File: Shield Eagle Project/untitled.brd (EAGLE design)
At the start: 160 x 100 mm, 5 parts, among them IC1 MCP4922-E_P, J1 61PC6F, Q1 TLP222A-2_F_, U1 ARDUINOR3-BPLACE

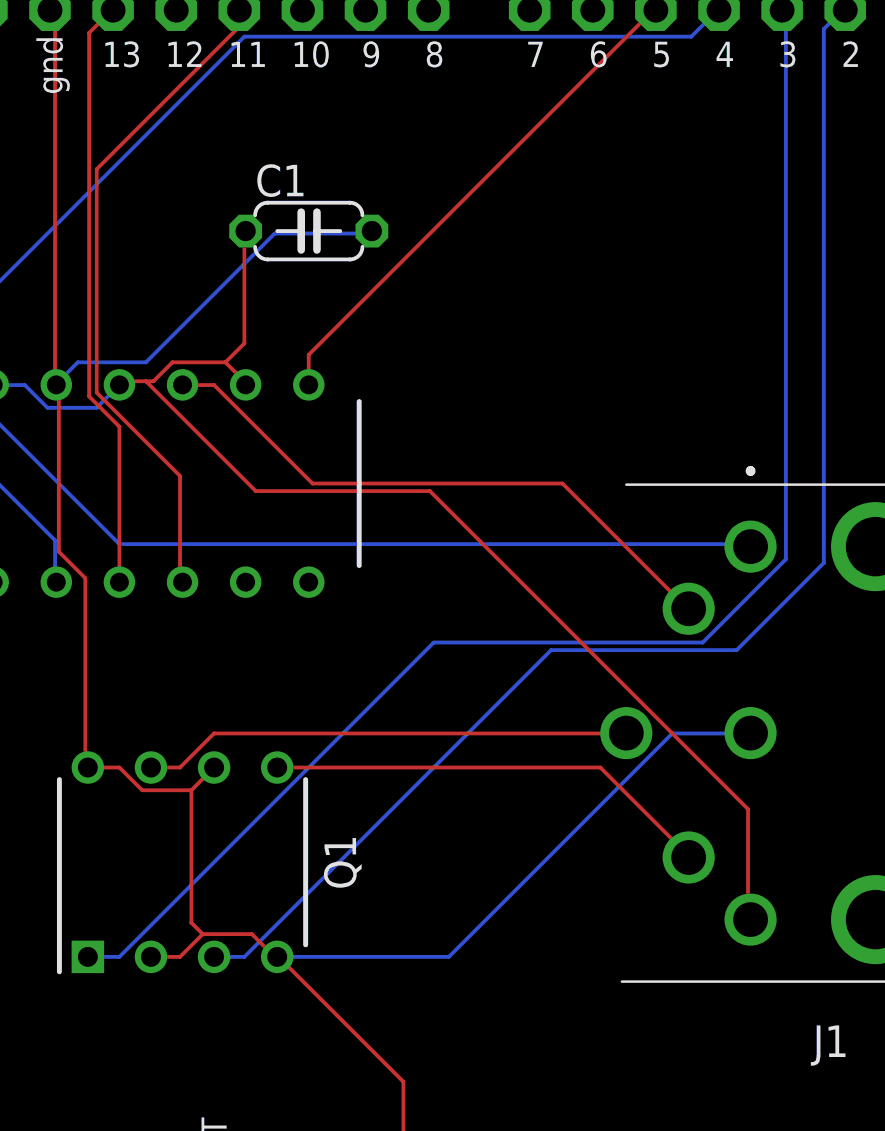
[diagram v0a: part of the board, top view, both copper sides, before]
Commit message: Add current limiting resistor for SSR to meet spec.
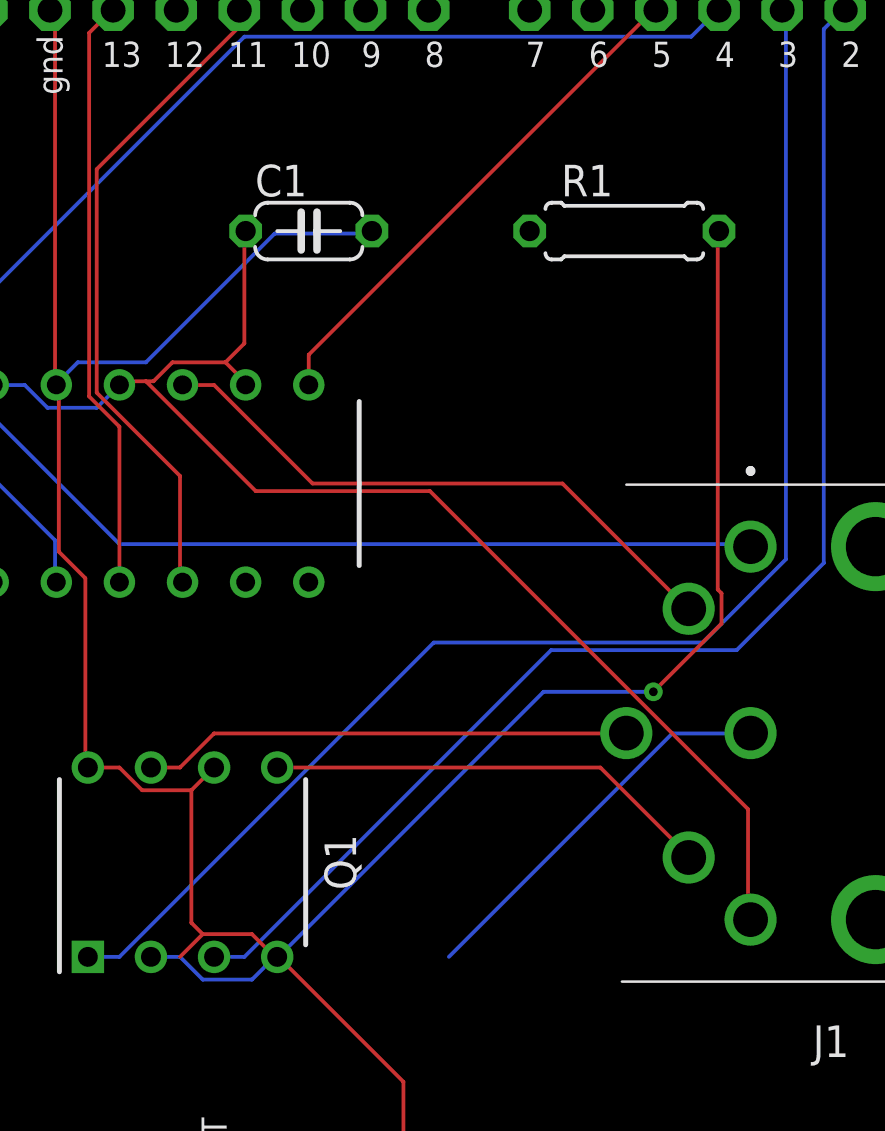
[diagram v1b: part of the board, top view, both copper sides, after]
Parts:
- added R1: 130 ohm, adafruit:0207/7
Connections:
- new net N$3: Q1.2, Q1.4, R1.2
- net GND: now also R1.1; no longer Q1.2, Q1.4
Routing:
- net N$3: track 0.00 -> 45.1 mm, vias 0 -> 1
- net GND: track 101.8 -> 93.6 mm
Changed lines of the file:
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@@
 <?xml version="1.0" encoding="utf-8"?>
 <!DOCTYPE eagle SYSTEM "eagle.dtd">
-<eagle version="9.6.1">
+<eagle version="9.6.2">
 <drawing>
 <settings>
@@
 <attribute name="VALUE" x="39.751" y="41.783" size="1.27" layer="27" ratio="10"/>
 </element>
+<element name="R1" library="adafruit" package="0207/7" value="130 ohm" x="54.61" y="44.45" smashed="yes">
+<attribute name="NAME" x="52.07" y="45.847" size="1.27" layer="25" ratio="10"/>
+<attribute name="VALUE" x="51.054" y="41.3512" size="1.27" layer="27" ratio="10"/>
+</element>
 </elements>
 <signals>
 <signal name="GND">
 <contactref element="U1" pad="GND1"/>
-<contactref element="Q1" pad="4"/>
-<contactref element="Q1" pad="2"/>
 <contactref element="IC1" pad="12"/>
 <contactref element="J1" pad="3"/>
@@
 <wire x1="48.1584" y1="5.1816" x2="45.72" y2="5.1816" width="0.1524" layer="1"/>
 <wire x1="48.1584" y1="5.1816" x2="48.26" y2="5.08" width="0.1524" layer="1"/>
-<wire x1="36.7284" y1="15.24" x2="35.56" y2="15.24" width="0.1524" layer="1"/>
 <wire x1="37.6428" y1="16.1544" x2="36.7284" y2="15.24" width="0.1524" layer="1"/>
 <wire x1="39.624" y1="16.1544" x2="37.6428" y2="16.1544" width="0.1524" layer="1"/>
 <wire x1="40.5384" y1="15.24" x2="39.624" y2="16.1544" width="0.1524" layer="1"/>
-<wire x1="40.5384" y1="15.24" x2="40.64" y2="15.24" width="0.1524" layer="1"/>
 <wire x1="45.72" y1="10.2108" x2="45.72" y2="5.1816" width="0.1524" layer="1"/>
 <wire x1="40.6908" y1="15.24" x2="45.72" y2="10.2108" width="0.1524" layer="1"/>
 <wire x1="45.72" y1="5.1816" x2="45.72" y2="5.08" width="0.1524" layer="1"/>
-<wire x1="40.6908" y1="15.24" x2="40.64" y2="15.24" width="0.1524" layer="1"/>
 <wire x1="56.5404" y1="24.2316" x2="59.5884" y2="24.2316" width="0.1524" layer="16"/>
 <wire x1="47.5488" y1="15.24" x2="56.5404" y2="24.2316" width="0.1524" layer="16"/>
-<wire x1="40.64" y1="15.24" x2="47.5488" y2="15.24" width="0.1524" layer="16"/>
 <wire x1="59.5884" y1="24.2316" x2="59.69" y2="24.245" width="0.1524" layer="16"/>
 <wire x1="37.1856" y1="16.6116" x2="37.1856" y2="21.9456" width="0.1524" layer="1"/>
@@
 <vertex x="5.08" y="2.54"/>
 </polygon>
+<contactref element="R1" pad="1"/>
 </signal>
 <signal name="VIN">
@@
 <wire x1="34.29" y1="38.2524" x2="34.29" y2="38.26" width="0.1524" layer="16"/>
 </signal>
+<signal name="N$3">
+<contactref element="Q1" pad="4"/>
+<contactref element="Q1" pad="2"/>
+<contactref element="R1" pad="2"/>
+<wire x1="36.7284" y1="15.24" x2="35.56" y2="15.24" width="0.1524" layer="16"/>
+<wire x1="37.6428" y1="14.3256" x2="36.7284" y2="15.24" width="0.1524" layer="16"/>
+<wire x1="39.624" y1="14.3256" x2="37.6428" y2="14.3256" width="0.1524" layer="16"/>
+<wire x1="40.5384" y1="15.24" x2="39.624" y2="14.3256" width="0.1524" layer="16"/>
+<wire x1="40.5384" y1="15.24" x2="40.64" y2="15.24" width="0.1524" layer="16"/>
+<wire x1="58.3692" y1="30.0228" x2="58.3692" y2="44.3484" width="0.1524" layer="1"/>
+<wire x1="58.5216" y1="29.8704" x2="58.3692" y2="30.0228" width="0.1524" layer="1"/>
+<wire x1="58.5216" y1="28.6512" x2="58.5216" y2="29.8704" width="0.1524" layer="1"/>
+<wire x1="55.7784" y1="25.908" x2="58.5216" y2="28.6512" width="0.1524" layer="1"/>
+<wire x1="51.3588" y1="25.908" x2="55.7784" y2="25.908" width="0.1524" layer="16"/>
+<wire x1="40.6908" y1="15.24" x2="51.3588" y2="25.908" width="0.1524" layer="16"/>
+<wire x1="58.3692" y1="44.3484" x2="58.42" y2="44.45" width="0.1524" layer="1"/>
+<wire x1="40.6908" y1="15.24" x2="40.64" y2="15.24" width="0.1524" layer="16"/>
+<via x="55.7784" y="25.908" extent="1-16" drill="0.35"/>
+</signal>
 </signals>

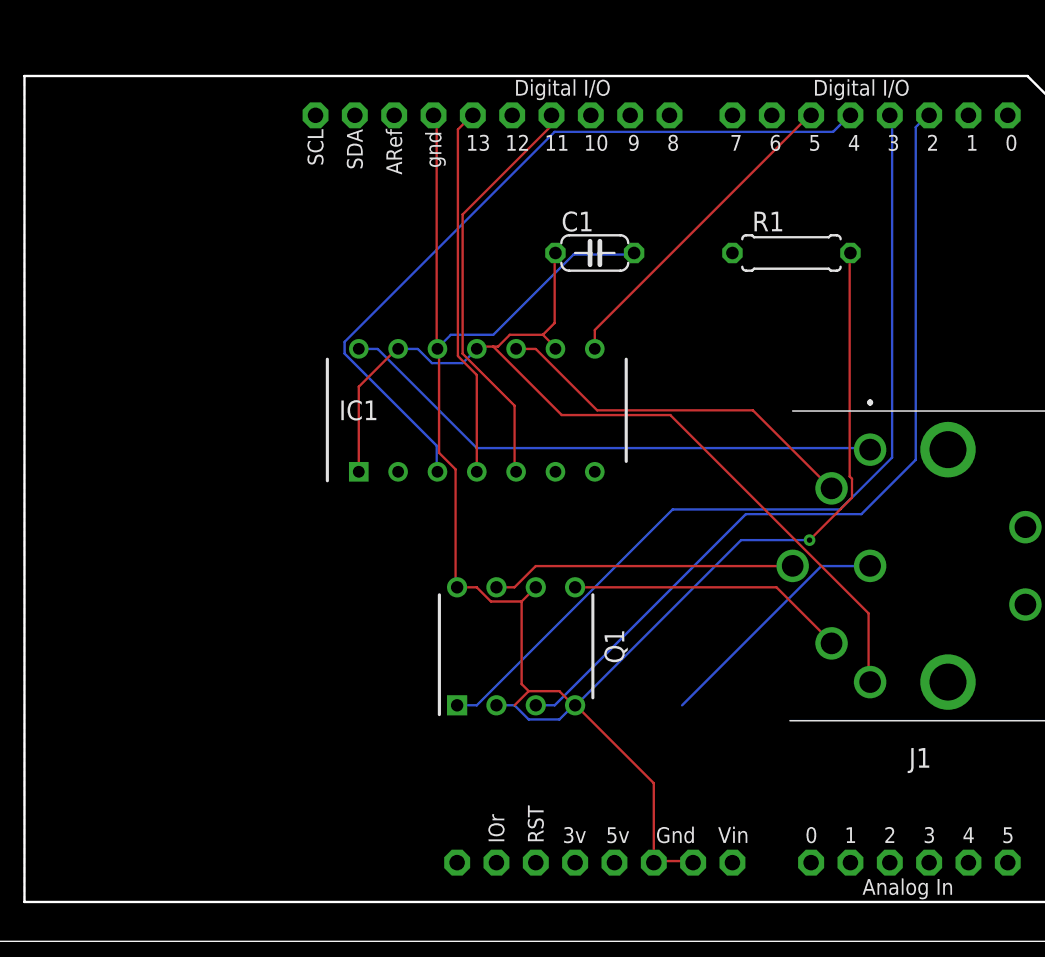
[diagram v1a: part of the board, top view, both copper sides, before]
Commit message: Using individual resistors between opto isolator and ground to avoid under current conditions that might have happened otherwise.
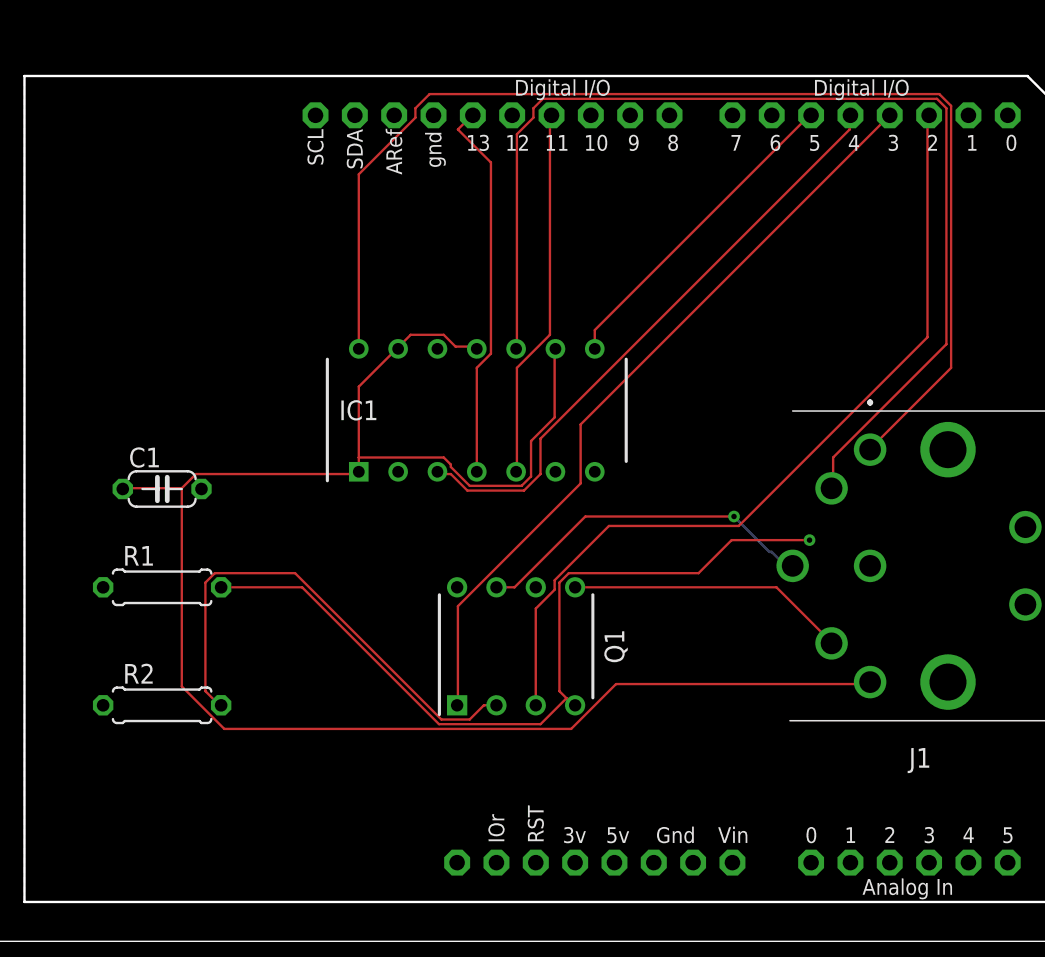
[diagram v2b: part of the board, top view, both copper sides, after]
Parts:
- added R2: 130 ohm, adafruit:0207/7
- moved R1 46.0 mm to (14.0, 22.9)
- moved C1 31.8 mm to (14.0, 29.2)
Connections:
- new net N$6: Q1.2, R2.2
- net GND: now also R2.1
- net N$3: no longer Q1.2
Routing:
- net GND: track 93.6 -> 0.51 mm
- net VCC: track 62.3 -> 111.8 mm
- net N$14: track 24.1 -> 70.9 mm
- net N$12: track 35.7 -> 76.8 mm
- net N$6: track 0.00 -> 31.7 mm
- net N$4: track 49.6 -> 39.2 mm
- net N$3: track 45.1 -> 52.4 mm
- net N$7: track 56.9 -> 49.7 mm
- net N$10: track 19.7 -> 22.3 mm, vias 0 -> 1
- net N$2: track 26.9 -> 24.9 mm
- net N$1: track 24.0 -> 24.7 mm
